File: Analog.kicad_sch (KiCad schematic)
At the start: 18 parts, among them U13 INA350

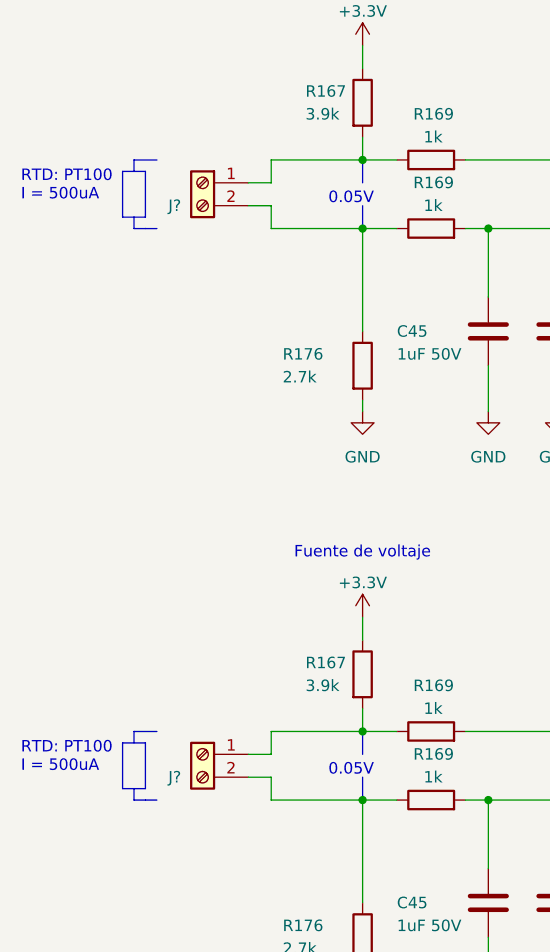
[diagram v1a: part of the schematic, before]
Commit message: SCH: Se modificó la posición de algunos pines para mejorar la calidad del ruteado. PCB: Se enruta las señales, quedando la alimentación, pines de programación, relays y planos de gnd
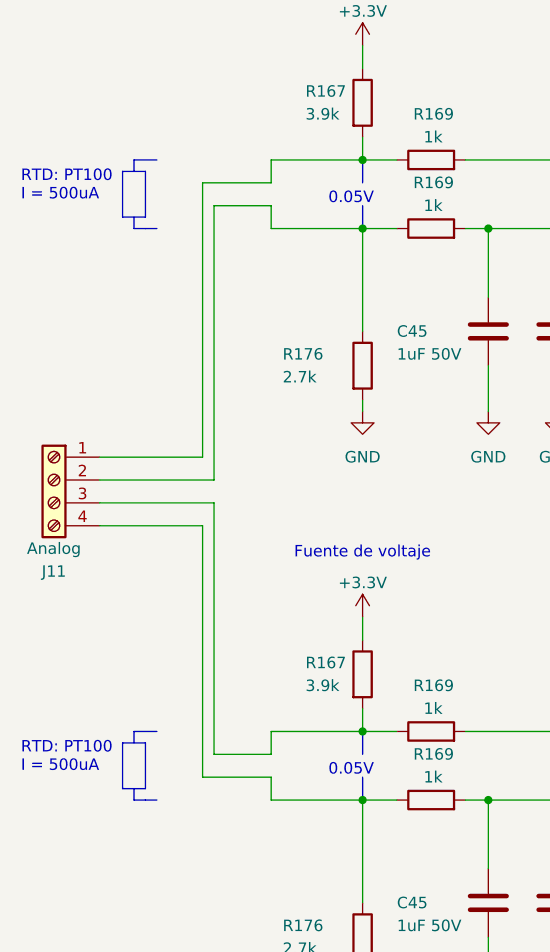
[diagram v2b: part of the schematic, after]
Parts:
- removed J? (x2): Screw_Terminal_01x02, 1-Terminal-Block:DG504-5.08-02P_or_SMKDS 2,5-2-5.08, symbol 1-Terminal-Block:DG504-5.08-02P
- added J11: Analog, 1-Terminal-Block:Terminal-Block_XY2500V-B_4P_P5.0mm_XINYA, symbol Connector:Screw_Terminal_01x04
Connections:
- net at R167.2, R169.1: now also J11.1 (Pin_1)
- net at R169.1, R176.1: now also J11.2 (Pin_2)
- net at R169.1, R176.1: now also J11.4 (Pin_4)
- net at R167.2, R169.1: now also J11.3 (Pin_3)
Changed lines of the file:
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@@
+    (stroke (width 0) (type default))
+  )
+  (wire (pts (xy 88.9 129.54) (xy 88.9 101.6))
+    (stroke (width 0) (type default))
+  )
+  (wire (pts (xy 77.47 93.98) (xy 88.9 93.98))
     (stroke (width 0) (type default))
   )
@@
     (stroke (width 0) (type default))
   )
-  (wire (pts (xy 93.98 127) (xy 96.52 127))
+  (wire (pts (xy 90.17 127) (xy 96.52 127))
     (stroke (width 0) (type default))
   )
@@
     (stroke (width 0) (type default))
   )
+  (wire (pts (xy 88.9 93.98) (xy 88.9 63.5))
+    (stroke (width 0) (type default))
+  )
   (polyline (pts (xy 82.55 132.08) (xy 83.82 132.08))
     (stroke (width 0) (type default))
@@
     (stroke (width 0) (type default))
   )
-  (wire (pts (xy 93.98 66.04) (xy 96.52 66.04))
+  (wire (pts (xy 90.17 66.04) (xy 96.52 66.04))
     (stroke (width 0) (type default))
   )
@@
     (stroke (width 0) (type default))
   )
-  (wire (pts (xy 93.98 63.5) (xy 96.52 63.5))
+  (wire (pts (xy 88.9 63.5) (xy 96.52 63.5))
     (stroke (width 0) (type default))
   )
@@
     (stroke (width 0) (type default))
   )
+  (wire (pts (xy 77.47 99.06) (xy 90.17 99.06))
+    (stroke (width 0) (type default))
+  )
   (wire (pts (xy 128.27 124.46) (xy 128.27 139.7))
     (stroke (width 0) (type default))
@@
     (stroke (width 0) (type default))
   )
+  (wire (pts (xy 77.47 101.6) (xy 88.9 101.6))
+    (stroke (width 0) (type default))
+  )
   (wire (pts (xy 118.11 60.96) (xy 128.27 60.96))
     (stroke (width 0) (type default))
@@
     (stroke (width 0) (type default))
   )
+  (wire (pts (xy 90.17 66.04) (xy 90.17 96.52))
+    (stroke (width 0) (type default))
+  )
   (wire (pts (xy 189.23 135.89) (xy 189.23 137.16))
     (stroke (width 0) (type default))
@@
     (stroke (width 0) (type default))
   )
+  (wire (pts (xy 90.17 99.06) (xy 90.17 127))
+    (stroke (width 0) (type default))
+  )
   (wire (pts (xy 120.65 132.08) (xy 137.16 132.08))
     (stroke (width 0) (type default))
@@
     (stroke (width 0) (type default))
   )
-  (wire (pts (xy 93.98 129.54) (xy 96.52 129.54))
+  (wire (pts (xy 88.9 129.54) (xy 96.52 129.54))
     (stroke (width 0) (type default))
   )
@@
   )
   (wire (pts (xy 96.52 66.04) (xy 96.52 68.58))
+    (stroke (width 0) (type default))
+  )
+  (wire (pts (xy 77.47 96.52) (xy 90.17 96.52))
     (stroke (width 0) (type default))
   )
@@
     )
   )
-  (symbol (lib_id "1-Terminal-Block:DG504-5.08-02P") (at 88.9 63.5 0) (mirror y) (unit 1)
-    (in_bom yes) (on_board yes) (dnp no)
-    (property "Reference" "J?" (at 85.09 66.04 0)
-      (effects (font (size 1.27 1.27)) (justify right))
-    )
-    (property "Value" "Screw_Terminal_01x02" (at 91.44 69.85 90)
-      (effects (font (size 1.27 1.27)) (justify right) hide)
-    )
-    (property "Footprint" "1-Terminal-Block:DG504-5.08-02P_or_SMKDS 2,5-2-5.08" (at 88.9 63.5 0)
-      (effects (font (size 1.27 1.27)) hide)
-    )
-    (property "Datasheet" "~" (at 88.9 63.5 0)
-      (effects (font (size 1.27 1.27)) hide)
-    )
-    (pin "1")
-    (pin "2")
-    (instances
-      (project "STM32_Esterilizador"
-        (path "/2e4bcfd0-2bd9-4947-aec4-3d35e12c1f92/fbe32eae-a32e-4dc8-97c1-9ed6fc94eaf5"
-          (reference "J?") (unit 1)
-        )
-        (path "/2e4bcfd0-2bd9-4947-aec4-3d35e12c1f92/9a001c70-a5ee-44c3-8e5d-6115c5f20be4"
-          (reference "J33") (unit 1)
-        )
-      )
-      (project "Controlador_Esterilizador_PCB"
-        (path "/8fbb718d-b37c-4149-8521-becf2eb363cd"
-          (reference "J?") (unit 1)
-        )
-        (path "/8fbb718d-b37c-4149-8521-becf2eb363cd/1d9fb762-9d81-4df8-a83c-aaca17042001"
-          (reference "J?") (unit 1)
-        )
-      )
-      (project "ConsorcioMedico_Refrigeradora"
-        (path "/e86bbed0-5bdc-4982-8297-fb5cecea731c/48dbbeb3-fee2-4df0-b8cf-5311531aaa2d"
-          (reference "J6") (unit 1)
-        )
-      )
-    )
-  )
   (symbol (lib_id "power:GND") (at 152.4 115.57 0) (unit 1)
     (in_bom yes) (on_board yes) (dnp no) (fields_autoplaced)
@@
     )
   )
-  (symbol (lib_id "1-Terminal-Block:DG504-5.08-02P") (at 88.9 127 0) (mirror y) (unit 1)
-    (in_bom yes) (on_board yes) (dnp no)
-    (property "Reference" "J?" (at 85.09 129.54 0)
-      (effects (font (size 1.27 1.27)) (justify right))
-    )
-    (property "Value" "Screw_Terminal_01x02" (at 91.44 133.35 90)
-      (effects (font (size 1.27 1.27)) (justify right) hide)
-    )
-    (property "Footprint" "1-Terminal-Block:DG504-5.08-02P_or_SMKDS 2,5-2-5.08" (at 88.9 127 0)
-      (effects (font (size 1.27 1.27)) hide)
-    )
-    (property "Datasheet" "~" (at 88.9 127 0)
-      (effects (font (size 1.27 1.27)) hide)
-    )
-    (pin "1")
-    (pin "2")
-    (instances
-      (project "STM32_Esterilizador"
-        (path "/2e4bcfd0-2bd9-4947-aec4-3d35e12c1f92/fbe32eae-a32e-4dc8-97c1-9ed6fc94eaf5"
-          (reference "J?") (unit 1)
-        )
-        (path "/2e4bcfd0-2bd9-4947-aec4-3d35e12c1f92/9a001c70-a5ee-44c3-8e5d-6115c5f20be4"
-          (reference "J34") (unit 1)
-        )
-      )
-      (project "Controlador_Esterilizador_PCB"
-        (path "/8fbb718d-b37c-4149-8521-becf2eb363cd"
-          (reference "J?") (unit 1)
-        )
-        (path "/8fbb718d-b37c-4149-8521-becf2eb363cd/1d9fb762-9d81-4df8-a83c-aaca17042001"
-          (reference "J?") (unit 1)
-        )
-      )
-      (project "ConsorcioMedico_Refrigeradora"
-        (path "/e86bbed0-5bdc-4982-8297-fb5cecea731c/48dbbeb3-fee2-4df0-b8cf-5311531aaa2d"
-          (reference "J7") (unit 1)
-        )
-      )
-    )
-  )
   (symbol (lib_id "power:GND") (at 189.23 76.2 0) (unit 1)
     (in_bom yes) (on_board yes) (dnp no) (fields_autoplaced)
@@
         )
       )
+    )
+  )
+  (symbol (lib_id "Connector:Screw_Terminal_01x04") (at 72.39 96.52 0) (mirror y) (unit 1)
+    (in_bom yes) (on_board yes) (dnp no)
+    (property "Reference" "J11" (at 72.39 106.68 0)
+      (effects (font (size 1.27 1.27)))
+    )
+    (property "Value" "Analog" (at 72.39 104.14 0)
+      (effects (font (size 1.27 1.27)))
+    )
+    (property "Footprint" "1-Terminal-Block:Terminal-Block_XY2500V-B_4P_P5.0mm_XINYA" (at 72.39 96.52 0)
+      (effects (font (size 1.27 1.27)) hide)
+    )
+    (property "Datasheet" "~" (at 72.39 96.52 0)
+      (effects (font (size 1.27 1.27)) hide)
+    )
+    (pin "1")
+    (pin "2")
+    (pin "3")
+    (pin "4")
+    (instances
+      (project "ConsorcioMedico_Refrigeradora"
+        (path "/e86bbed0-5bdc-4982-8297-fb5cecea731c/80a96d94-2098-4e0a-a173-fbb6709c7b1a"
+          (reference "J11") (unit 1)
+        )
+        (path "/e86bbed0-5bdc-4982-8297-fb5cecea731c/48dbbeb3-fee2-4df0-b8cf-5311531aaa2d"
+          (reference "J16") (unit 1)
+        )
+      )

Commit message: Luego de modificaciones de Dandy
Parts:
- added R60, R62: 10k, 1-Resistor:R_0805_2012Metric, symbol 1-Resistor:R_0805
- added R61, R63: 910R, 1-Resistor:R_0805_2012Metric, symbol 1-Resistor:R_0805
- R167: value 3.9k -> 10k
- R176: value 2.7k -> 1k
- renumbered J11 to J16
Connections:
- net +3.3V: now also R60.1, R62.1
- net at J16.2 (Pin_2), R176.1: now also R61.2; no longer R169.1
- net at J16.4 (Pin_4), R176.1: now also R63.2; no longer R169.1
- new net: R169.1, R60.2, R61.1
- new net: R169.1, R62.2, R63.1
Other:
- note added: "-10grados 960.9ohm = 11.87mV = X20 =237.4mV 40 grados 1155ohm = 56.24mV = X20 = 1124.8mV"
- note added: "100 to 300uA PT1000"
- note added: "OPEN G=20"
- note added: "RTD: PT1000 I = 250uA"
- note removed: "0.05V"
- note removed: "RTD: PT100 I = 500uA"
- moved on the sheet: J16, R167, R176
